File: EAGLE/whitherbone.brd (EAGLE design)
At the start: 86.4 x 54.6 mm, 224 parts, among them IC10 TXS0108ERGYR, IC11 TXS0108ERGYR, IC12 TPS2051BDGN, IC13 SN74AUC1G74, IC14 TPD4S012DRY, IC15 TPD4S012DRY, IC17 SN74LVC2G241DCUR, IC18 TL1963ADCQR, IC19 AP2112K-1.8TRG1 3.3V, IC2 SN74LVC1G07DCK, IC4 7805T, IC7 IP4283CZ10-TBR, IC8 IP4283CZ10-TBR, IC9 TDA19988BHN/C1,557, Q2 32.768kHz, Q4 24 MHz, T3 BSS138W-7-F, T4 BSS138W-7-F, U1 OSD3358-512M-BSM, X2 SCHA5B0200, X4 10118192-0001LF

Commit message: Connected WiFi/BT
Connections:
- net XDMA_EVENT_INTRO renamed XDMA_EVENT_INTR0
- net N$3: now also U1.A4
- net SD.CD: now also U1.C14
- net SD.CLK: now also U1.B15
- net SD.CMD: now also U1.B16
- net SD.D0: now also U1.A16
- net SD.D1: now also U1.A15
- net SD.D2: now also U1.C16
- net SD.D3: now also U1.C15
- net UART0_RXD: now also U1.A12
- net UART0_TXD: now also U1.B12
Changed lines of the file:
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@@
 <wire x1="81.0006" y1="37.4904" x2="81.0006" y2="37.9476" width="0.1524" layer="3"/>
 <wire x1="81.0006" y1="37.9476" x2="82.677" y2="39.624" width="0.1524" layer="3"/>
+<contactref element="U1" pad="C15"/>
+<wire x1="82.29520625" y1="44.969" x2="45.5168" y2="78.8416" width="0" layer="19" extent="1-16"/>
 </signal>
 <signal name="SD.D1">
@@
 <wire x1="70.5612" y1="10.2108" x2="70.5612" y2="11.1252" width="0.1524" layer="3"/>
 <wire x1="70.5612" y1="11.1252" x2="70.2564" y2="11.43" width="0.1524" layer="3"/>
+<contactref element="U1" pad="A15"/>
+<wire x1="79.8576" y1="32.385" x2="42.9768" y2="78.8416" width="0" layer="19" extent="1-3"/>
 </signal>
 <signal name="SD.D0">
@@
 <wire x1="73.6092" y1="7.62" x2="70.866" y2="10.3632" width="0.1524" layer="3"/>
 <wire x1="70.866" y1="12.3444" x2="70.866" y2="10.3632" width="0.1524" layer="3"/>
+<contactref element="U1" pad="A16"/>
+<wire x1="81.8896" y1="35.179" x2="42.9768" y2="80.1116" width="0" layer="19" extent="1-3"/>
 </signal>
 <signal name="SD.D2">
@@
 <wire x1="82.0674" y1="39.4716" x2="82.0674" y2="40.0304" width="0.1524" layer="3"/>
 <wire x1="82.0674" y1="40.0304" x2="82.677" y2="40.64" width="0.1524" layer="3"/>
+<contactref element="U1" pad="C16"/>
+<wire x1="81.59520625" y1="44.969" x2="45.5168" y2="80.1116" width="0" layer="19" extent="1-16"/>
 </signal>
 <signal name="SD.CLK">
@@
 <wire x1="83.5914" y1="35.5346" x2="82.677" y2="36.449" width="0.1524" layer="16"/>
 <wire x1="82.677" y1="36.449" x2="82.677" y2="36.957" width="0.1524" layer="16"/>
+<contactref element="U1" pad="B15"/>
+<wire x1="82.677" y1="36.957" x2="44.2468" y2="78.8416" width="0" layer="19" extent="1-1"/>
 </signal>
 <signal name="SD.CMD">
@@
 <wire x1="83.447" y1="38.989" x2="82.931" y2="38.989" width="0.1524" layer="1"/>
 <wire x1="82.931" y1="38.989" x2="82.677" y2="38.735" width="0.1524" layer="1"/>
+<contactref element="U1" pad="B16"/>
+<wire x1="82.99520625" y1="44.969" x2="44.2468" y2="80.1116" width="0" layer="19" extent="1-16"/>
 </signal>
 <signal name="N$16">
@@
 <wire x1="36.957" y1="18.161" x2="39.6748" y2="18.161" width="0.1524" layer="14"/>
 <wire x1="39.6748" y1="18.161" x2="40.9956" y2="16.8402" width="0.1524" layer="14"/>
+<contactref element="U1" pad="C14"/>
+<wire x1="71.61020625" y1="43.694" x2="45.5168" y2="77.5716" width="0" layer="19" extent="1-16"/>
 </signal>
 <signal name="PMIC_PGOOD">
@@
 <wire x1="34.29" y1="14.224" x2="35.2298" y2="14.224" width="0.1524" layer="3"/>
 <wire x1="35.2298" y1="14.224" x2="39.5478" y2="9.906" width="0.1524" layer="3"/>
-</signal>
-<signal name="XDMA_EVENT_INTRO">
+<contactref element="U1" pad="A4"/>
+<wire x1="35.568" y1="14.224" x2="42.9768" y2="64.8716" width="0" layer="19" extent="1-1"/>
+</signal>
+<signal name="XDMA_EVENT_INTR0">
 <contactref element="FB5" pad="2"/>
 <contactref element="IC13" pad="1"/>
@@
 <wire x1="45.478" y1="14.871" x2="45.466" y2="14.859" width="0.1524" layer="16"/>
 <wire x1="45.466" y1="14.986" x2="45.466" y2="14.859" width="0.1524" layer="1"/>
+<contactref element="U1" pad="B12"/>
+<wire x1="45.466" y1="14.986" x2="44.2468" y2="75.0316" width="0" layer="19" extent="1-1"/>
 </signal>
 <signal name="UART0_RXD">
@@
 <wire x1="45.843" y1="15.371" x2="45.466" y2="15.748" width="0.1524" layer="16"/>
 <wire x1="45.466" y1="15.748" x2="45.466" y2="16.383" width="0.1524" layer="16"/>
+<contactref element="U1" pad="A12"/>
+<wire x1="45.466" y1="16.383" x2="42.9768" y2="75.0316" width="0" layer="19" extent="1-1"/>
 </signal>
 <signal name="N$54">

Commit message: Connected WiFi/BT
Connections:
- net BT_EN.SIP: now also U1.H15
- net BT_HCI_CTS.SIP: now also U1.E13
- net BT_HCI_RTS.SIP: now also U1.D13
- net BT_HCI_RX.SIP: now also U1.D14
- net BT_HCI_TX.SIP: now also U1.D15
- net LS_BUF_OE: now also U1.E16
- net MCU.LCD.CLK: now also U1.F1
- net MCU.LCD.EN: now also U1.E1
- net MCU.LCD.HS: now also U1.F2
- net MCU.LCD.VS: now also U1.F3
- net WL_EN.SIP: now also U1.H16
- net WL_IRQ.SIP: now also U1.H14
- net WL_SDIO_CLK.SIP: now also U1.D16
- net WL_SDIO_CMD.SIP: now also U1.G14
- net WL_SDIO_D0.SIP: now also U1.F16
- net WL_SDIO_D1.SIP: now also U1.G15
- net WL_SDIO_D2.SIP: now also U1.G16
- net WL_SDIO_D3.SIP: now also U1.F15
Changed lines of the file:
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@@
 <wire x1="41.3004" y1="23.0886" x2="36.5624" y2="23.0886" width="0.1524" layer="16"/>
 <wire x1="36.5624" y1="23.0886" x2="34.378" y2="25.273" width="0.1524" layer="16"/>
+<contactref element="U1" pad="E16"/>
+<wire x1="34.378" y1="25.273" x2="48.0568" y2="80.1116" width="0" layer="19" extent="1-16"/>
 </signal>
 <signal name="BT_HCI_TX.SIP">
@@
 <wire x1="30.6324" y1="23.622" x2="30.2544" y2="24" width="0.1524" layer="15"/>
 <wire x1="30.2544" y1="24" x2="29.25" y2="24" width="0.1524" layer="15"/>
+<contactref element="U1" pad="D15"/>
+<wire x1="36.7284" y1="25.7556" x2="46.7868" y2="78.8416" width="0" layer="19" extent="1-16"/>
 </signal>
 <signal name="BT_HCI_RX.SIP">
@@
 <wire x1="31.5468" y1="27.8892" x2="31.5468" y2="24.4348" width="0.1524" layer="14"/>
 <wire x1="31.5468" y1="24.4348" x2="31.3436" y2="24.2316" width="0.1524" layer="14"/>
+<contactref element="U1" pad="D14"/>
+<wire x1="30.5562" y1="28.8798" x2="46.7868" y2="77.5716" width="0" layer="19" extent="1-14"/>
 </signal>
 <signal name="BT_HCI_RTS.SIP">
@@
 <wire x1="28.0416" y1="29.718" x2="28.575" y2="30.2514" width="0.1524" layer="1"/>
 <wire x1="28.575" y1="30.2514" x2="28.575" y2="30.869" width="0.1524" layer="1"/>
+<contactref element="U1" pad="D13"/>
+<wire x1="28.575" y1="30.869" x2="46.7868" y2="76.3016" width="0" layer="19" extent="1-1"/>
 </signal>
 <signal name="BT_HCI_CTS.SIP">
@@
 <wire x1="28.6512" y1="28.2702" x2="28.6512" y2="29.6752" width="0.1524" layer="1"/>
 <wire x1="28.6512" y1="29.6752" x2="29.845" y2="30.869" width="0.1524" layer="1"/>
+<contactref element="U1" pad="E13"/>
+<wire x1="29.845" y1="30.869" x2="48.0568" y2="76.3016" width="0" layer="19" extent="1-1"/>
 </signal>
 <signal name="I2C0_SDA">
@@
 <wire x1="55.245" y1="43.5864" x2="55.245" y2="44.958" width="0.1524" layer="1"/>
 <wire x1="59.1312" y1="39.7764" x2="59.5122" y2="40.1574" width="0.1524" layer="16"/>
+<contactref element="U1" pad="F1"/>
+<wire x1="55.245" y1="46.998" x2="49.3268" y2="61.0616" width="0" layer="19" extent="1-1"/>
 </signal>
 <signal name="MCU.LCD.VS">
@@
 <wire x1="54.9402" y1="43.434" x2="54.9402" y2="44.8056" width="0.1524" layer="1"/>
 <wire x1="59.436" y1="38.862" x2="60.1218" y2="39.5478" width="0.1524" layer="16"/>
+<contactref element="U1" pad="F3"/>
+<wire x1="53.975" y1="46.998" x2="49.3268" y2="63.6016" width="0" layer="19" extent="1-1"/>
 </signal>
 <signal name="MCU.LCD.HS">
@@
 <wire x1="59.3344" y1="45.9486" x2="59.055" y2="46.228" width="0.1524" layer="16"/>
 <wire x1="65.8368" y1="44.8818" x2="65.8368" y2="40.9956" width="0.1524" layer="16"/>
+<contactref element="U1" pad="F2"/>
+<wire x1="56.515" y1="46.998" x2="49.3268" y2="62.3316" width="0" layer="19" extent="1-1"/>
 </signal>
 <signal name="MCU.LCD.EN">
@@
 <wire x1="66.4464" y1="40.6908" x2="68.0092" y2="40.6908" width="0.1524" layer="16"/>
 <wire x1="68.0092" y1="40.6908" x2="69.05" y2="39.65" width="0.1524" layer="16"/>
+<contactref element="U1" pad="E1"/>
+<wire x1="66.4464" y1="40.6908" x2="48.0568" y2="61.0616" width="0" layer="19" extent="1-16"/>
 </signal>
 <signal name="N$45">
@@
 <wire x1="31.7754" y1="28.8798" x2="32.385" y2="28.2702" width="0.1524" layer="16"/>
 <wire x1="32.385" y1="28.2702" x2="35.1282" y2="28.2702" width="0.1524" layer="16"/>
+<contactref element="U1" pad="F16"/>
+<wire x1="35.1282" y1="28.2702" x2="49.3268" y2="80.1116" width="0" layer="19" extent="1-16"/>
 </signal>
 <signal name="WL_SDIO_D1.SIP">
@@
 <wire x1="32.678" y1="28.575" x2="35.2806" y2="28.575" width="0.1524" layer="16"/>
 <wire x1="35.2806" y1="28.575" x2="36.4236" y2="27.432" width="0.1524" layer="16"/>
+<contactref element="U1" pad="G15"/>
+<wire x1="35.2806" y1="28.575" x2="50.5968" y2="78.8416" width="0" layer="19" extent="1-16"/>
 </signal>
 <signal name="WL_SDIO_D2.SIP">
@@
 <wire x1="34.4052" y1="28.8798" x2="35.814" y2="28.8798" width="0.1524" layer="16"/>
 <wire x1="35.814" y1="28.8798" x2="36.6522" y2="28.0416" width="0.1524" layer="16"/>
+<contactref element="U1" pad="G16"/>
+<wire x1="38.1" y1="28.6512" x2="50.5968" y2="80.1116" width="0" layer="19" extent="1-14"/>
 </signal>
 <signal name="WL_SDIO_D3.SIP">
@@
 <wire x1="37.2618" y1="28.6512" x2="37.8714" y2="28.0416" width="0.1524" layer="16"/>
 <wire x1="38.2524" y1="28.0416" x2="37.8714" y2="28.0416" width="0.1524" layer="14"/>
+<contactref element="U1" pad="F15"/>
+<wire x1="35.56" y1="29.63" x2="49.3268" y2="78.8416" width="0" layer="19" extent="1-16"/>
 </signal>
 <signal name="WL_SDIO_CLK.SIP">
@@
 <wire x1="46.951" y1="24.003" x2="46.951" y2="22.821" width="0.1524" layer="16"/>
 <wire x1="46.951" y1="22.821" x2="46.736" y2="22.606" width="0.1524" layer="16"/>
+<contactref element="U1" pad="D16"/>
+<wire x1="46.951" y1="24.003" x2="46.7868" y2="80.1116" width="0" layer="19" extent="1-16"/>
 </signal>
 <signal name="WL_SDIO_CMD.SIP">
@@
 <wire x1="42.8244" y1="24.384" x2="38.1" y2="29.1084" width="0.1524" layer="14"/>
 <wire x1="38.1" y1="29.1084" x2="38.1" y2="31.0896" width="0.1524" layer="14"/>
+<contactref element="U1" pad="G14"/>
+<wire x1="32.9574" y1="38.481" x2="50.5968" y2="77.5716" width="0" layer="19" extent="1-16"/>
 </signal>
 <signal name="WL_EN.SIP">
@@
 <wire x1="34.378" y1="21.209" x2="35.3432" y2="22.1742" width="0.1524" layer="16"/>
 <wire x1="35.3432" y1="22.1742" x2="40.0812" y2="22.1742" width="0.1524" layer="16"/>
+<contactref element="U1" pad="H16"/>
+<wire x1="40.0812" y1="22.1742" x2="51.8668" y2="80.1116" width="0" layer="19" extent="1-16"/>
 </signal>
 <signal name="BT_EN.SIP">
@@
 <wire x1="40.2336" y1="22.479" x2="35.14" y2="22.479" width="0.1524" layer="16"/>
 <wire x1="35.14" y1="22.479" x2="34.378" y2="23.241" width="0.1524" layer="16"/>
+<contactref element="U1" pad="H15"/>
+<wire x1="40.2336" y1="22.479" x2="51.8668" y2="78.8416" width="0" layer="19" extent="1-16"/>
 </signal>
 <signal name="WL_IRQ.SIP">
@@
 <wire x1="34.378" y1="19.177" x2="37.0704" y2="21.8694" width="0.1524" layer="16"/>
 <wire x1="37.0704" y1="21.8694" x2="39.9288" y2="21.8694" width="0.1524" layer="16"/>
+<contactref element="U1" pad="H14"/>
+<wire x1="39.9288" y1="21.8694" x2="51.8668" y2="77.5716" width="0" layer="19" extent="1-16"/>
 </signal>
 <signal name="N$25">

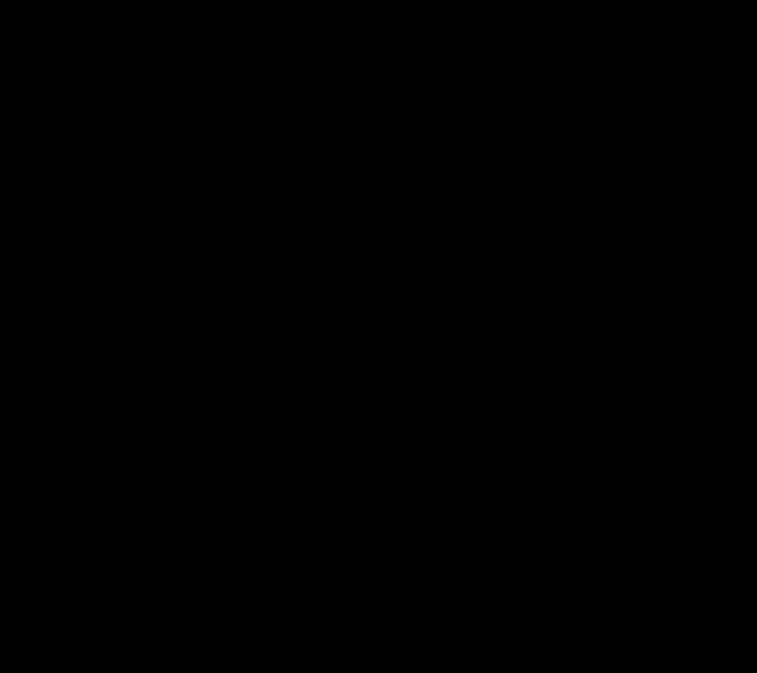
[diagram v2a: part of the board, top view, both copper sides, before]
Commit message: Add HDMI
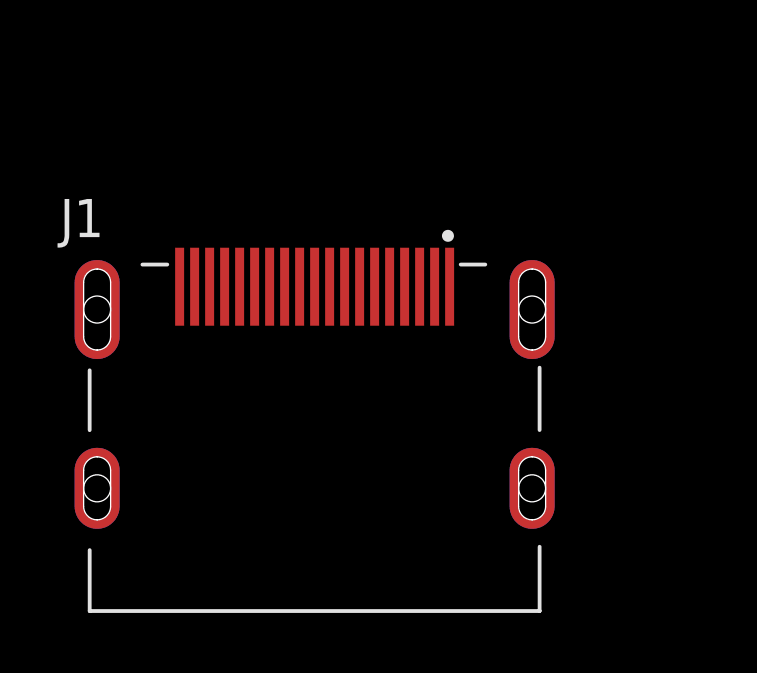
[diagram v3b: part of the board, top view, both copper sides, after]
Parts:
- added J1: 1-1747981-1, 1-1747981-1:TE_1-1747981-1
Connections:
- net CEC: now also J1.7
- net DVI_5V: now also J1.2
- net GND: now also J1.12, J1.15, J1.18, J1.3, J1.6, J1.9
- net HDMI.DSCL: now also J1.5
- net HDMI.DSDA: now also J1.4
- net HPD: now also J1.1
- net TX0+: now also J1.13
- net TX0-: now also J1.11
- net TX1+: now also J1.16
- net TX1-: now also J1.14
- net TX2+: now also J1.19
- net TX2-: now also J1.17
- net TXC+: now also J1.10
- net TXC-: now also J1.8
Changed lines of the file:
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@@
 <element name="U1" library="PocketBeagle" library_urn="urn:adsk.eagle:library:379102" package="OSD335X-BGA-256" package3d_urn="urn:adsk.eagle:package:379214/2" value="OSD3358-512M-BSM" x="52.5018" y="70.5866"/>
 <element name="IC4" library="linear" library_urn="urn:adsk.eagle:library:262" package="TO220H" package3d_urn="urn:adsk.eagle:package:16414/1" value="7805T" x="-27.2288" y="-29.0576"/>
+<element name="J1" library="1-1747981-1" package="TE_1-1747981-1" value="1-1747981-1" x="-28.8798" y="-55.88">
+<attribute name="AVAILABILITY" value="Good" x="-28.8798" y="-55.88" size="1.778" layer="27" display="off"/>
+<attribute name="CENTERLINE_PITCH" value="1 mm[.039 in]" x="-28.8798" y="-55.88" size="1.778" layer="27" display="off"/>
+<attribute name="COMMENT" value="1-1747981-1" x="-28.8798" y="-55.88" size="1.778" layer="27" display="off"/>
+<attribute name="DESCRIPTION" value=" TRAY PACKAGE HDMI CONNECTOR SMT " x="-28.8798" y="-55.88" size="1.778" layer="27" display="off"/>
+<attribute name="MF" value="TE Connectivity" x="-28.8798" y="-55.88" size="1.778" layer="27" display="off"/>
+<attribute name="MP" value="1-1747981-1" x="-28.8798" y="-55.88" size="1.778" layer="27" display="off"/>
+<attribute name="NUMBER_OF_POSITIONS" value="19" x="-28.8798" y="-55.88" size="1.778" layer="27" display="off"/>
+<attribute name="PACKAGE" value="None" x="-28.8798" y="-55.88" size="1.778" layer="27" display="off"/>
+<attribute name="PRICE" value="2.97 USD" x="-28.8798" y="-55.88" size="1.778" layer="27" display="off"/>
+<attribute name="PRODUCT_TYPE" value="Connector" x="-28.8798" y="-55.88" size="1.778" layer="27" display="off"/>
+</element>
 </elements>
 <signals>
@@
 <contactref element="U1" pad="J5"/>
 <contactref element="U1" pad="J4"/>
+<contactref element="J1" pad="15"/>
+<contactref element="J1" pad="18"/>
+<contactref element="J1" pad="3"/>
+<contactref element="J1" pad="6"/>
+<contactref element="J1" pad="9"/>
+<contactref element="J1" pad="12"/>
 <wire x1="56.9468" y1="73.7616" x2="56.9468" y2="75.0316" width="0" layer="19" extent="1-1"/>
 <wire x1="56.9468" y1="72.4916" x2="56.9468" y2="73.7616" width="0" layer="19" extent="1-1"/>
@@
 <wire x1="3.898" y1="9.525" x2="4.31" y2="17.653" width="0" layer="19" extent="1-16"/>
 <wire x1="-27.2288" y1="-39.2176" x2="3.898" y2="9.525" width="0" layer="19" extent="16-16"/>
+<wire x1="-26.8798" y1="-50.845" x2="-27.2288" y2="-39.2176" width="0" layer="19" extent="1-1"/>
+<wire x1="-28.3798" y1="-50.845" x2="-26.8798" y2="-50.845" width="0" layer="19" extent="1-1"/>
+<wire x1="-29.8798" y1="-50.845" x2="-28.3798" y2="-50.845" width="0" layer="19" extent="1-1"/>
+<wire x1="-31.3798" y1="-50.845" x2="-29.8798" y2="-50.845" width="0" layer="19" extent="1-1"/>
+<wire x1="-32.8798" y1="-50.845" x2="-31.3798" y2="-50.845" width="0" layer="19" extent="1-1"/>
+<wire x1="-25.3798" y1="-50.845" x2="-26.8798" y2="-50.845" width="0" layer="19" extent="1-1"/>
 </signal>
 <signal name="N$6">
@@
 <wire x1="66.801" y1="18.542" x2="66.801" y2="20.448" width="0.8128" layer="16"/>
 <wire x1="66.801" y1="20.448" x2="66.548" y2="20.701" width="0.8128" layer="16"/>
+<contactref element="J1" pad="2"/>
+<wire x1="-24.8798" y1="-50.845" x2="66.801" y2="18.542" width="0" layer="19" extent="1-16"/>
 </signal>
 <signal name="HDMI.DSDA">
@@
 <wire x1="70.35" y1="30.45" x2="69.9" y2="30" width="0.1524" layer="1"/>
 <wire x1="82.194146875" y1="26.745946875" x2="82.423" y2="26.9748" width="0.1524" layer="16"/>
+<contactref element="J1" pad="4"/>
+<wire x1="-25.8798" y1="-50.845" x2="69.0372" y2="27.5082" width="0" layer="19" extent="1-16"/>
 </signal>
 <signal name="HDMI.DSCL">
@@
 <wire x1="71.628" y1="28.622" x2="71.628" y2="27.2034" width="0.1524" layer="16"/>
 <wire x1="71.628" y1="27.2034" x2="72.285353125" y2="26.546046875" width="0.1524" layer="16"/>
+<contactref element="J1" pad="5"/>
+<wire x1="-26.3798" y1="-50.845" x2="71.628" y2="27.2034" width="0" layer="19" extent="1-16"/>
 </signal>
 <signal name="EXT_SWING">
@@
 <wire x1="74.8656" y1="30.9" x2="69.55" y2="30.9" width="0.1524" layer="3"/>
 <wire x1="78.9432" y1="22.86" x2="79.429103125" y2="23.345903125" width="0.1524" layer="16"/>
+<contactref element="J1" pad="1"/>
+<wire x1="-24.3798" y1="-50.845" x2="69.55" y2="30.9" width="0" layer="19" extent="1-1"/>
 </signal>
 <signal name="CEC">
@@
 <wire x1="69.503" y1="27.339" x2="69.088" y2="27.339" width="0.1524" layer="1"/>
 <wire x1="71.923403125" y1="26.145996875" x2="71.0946" y2="26.9748" width="0.1524" layer="16"/>
+<contactref element="J1" pad="7"/>
+<wire x1="-27.3798" y1="-50.845" x2="69.088" y2="27.339" width="0" layer="19" extent="1-1"/>
 </signal>
 <signal name="N$66">
@@
 <wire x1="71.2" y1="19.6" x2="70.95" y2="19.35" width="0.1524" layer="16"/>
 <wire x1="78.6384" y1="23.0124" x2="79.371953125" y2="23.745953125" width="0.1524" layer="16"/>
+<contactref element="J1" pad="19"/>
+<wire x1="-33.3798" y1="-50.845" x2="70.1875" y2="19.7" width="0" layer="19" extent="1-16"/>
 </signal>
 <signal name="TX2-">
@@
 <wire x1="71.2" y1="20" x2="70.95" y2="20.25" width="0.1524" layer="16"/>
 <wire x1="78.3336" y1="23.1648" x2="79.314803125" y2="24.146003125" width="0.1524" layer="16"/>
+<contactref element="J1" pad="17"/>
+<wire x1="-32.3798" y1="-50.845" x2="70.1875" y2="20.2" width="0" layer="19" extent="1-16"/>
 </signal>
 <signal name="TX1+">
@@
 <wire x1="71.2" y1="21.4" x2="70.95" y2="21.15" width="0.1524" layer="14"/>
 <wire x1="81.9912" y1="24.5364" x2="81.8007" y2="24.3459" width="0.1524" layer="16"/>
+<contactref element="J1" pad="16"/>
+<wire x1="-31.8798" y1="-50.845" x2="70.1875" y2="21.2" width="0" layer="19" extent="1-16"/>
 </signal>
 <signal name="TX1-">
@@
 <wire x1="71.2" y1="21.8" x2="70.95" y2="22.05" width="0.1524" layer="14"/>
 <wire x1="81.8388" y1="24.8412" x2="81.74355" y2="24.74595" width="0.1524" layer="16"/>
+<contactref element="J1" pad="14"/>
+<wire x1="-30.8798" y1="-50.845" x2="70.1875" y2="21.7" width="0" layer="19" extent="1-16"/>
 </signal>
 <signal name="TX0+">
@@
 <wire x1="72.712" y1="23.3" x2="74.5998" y2="21.4122" width="0.1524" layer="16"/>
 <wire x1="78.0288" y1="24.5364" x2="78.438503125" y2="24.946103125" width="0.1524" layer="16"/>
+<contactref element="J1" pad="13"/>
+<wire x1="-30.3798" y1="-50.845" x2="70.1875" y2="23.4" width="0" layer="19" extent="1-16"/>
 </signal>
 <signal name="TX0-">
@@
 <wire x1="72.7692" y1="23.7" x2="74.7522" y2="21.717" width="0.1524" layer="16"/>
 <wire x1="77.724" y1="24.6888" x2="78.381096875" y2="25.345896875" width="0.1524" layer="16"/>
+<contactref element="J1" pad="11"/>
+<wire x1="-29.3798" y1="-50.845" x2="70.1875" y2="23.9" width="0" layer="19" extent="1-16"/>
 </signal>
 <signal name="TXC+">
@@
 <wire x1="71.2" y1="25.1" x2="70.95" y2="24.85" width="0.1524" layer="14"/>
 <wire x1="81.8388" y1="25.4508" x2="81.74355" y2="25.54605" width="0.1524" layer="16"/>
+<contactref element="J1" pad="10"/>
+<wire x1="-28.8798" y1="-50.845" x2="70.1875" y2="24.9" width="0" layer="19" extent="1-16"/>
 </signal>
 <signal name="TXC-">
@@
 <wire x1="71.2" y1="25.5" x2="70.95" y2="25.75" width="0.1524" layer="14"/>
 <wire x1="81.9912" y1="25.7556" x2="81.8007" y2="25.9461" width="0.1524" layer="16"/>
+<contactref element="J1" pad="8"/>
+<wire x1="-27.8798" y1="-50.845" x2="70.1875" y2="25.4" width="0" layer="19" extent="1-16"/>
 </signal>
 <signal name="VBUS.HOST">
